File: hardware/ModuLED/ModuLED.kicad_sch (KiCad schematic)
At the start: 0 parts

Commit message: kicad
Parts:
- added D1, D10, D11, D12, D13, D14, D15, D16, D17, D18, D19, D2, D20, D21, D22, D23, D24, D25, D26, D27, D28, D29, D3, D30, D31, D32, D33, D34, D35, D36, D37, D38, D39, D4, D40, D41, D42, D43, D44, D45, D46, D47, D48, D49, D5, D50, D51, D52, D53, D54, D55, D56, D6, D7, D8, D9: LED, LED_THT:LED_D3.0mm_Clear, symbol Device:LED
- added U1: MAX7219, symbol Driver_LED:MAX7219
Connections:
- new net: D1.2 (A), D2.2 (A), D3.2 (A), D4.2 (A), D5.2 (A), D6.2 (A), D7.2 (A)
- new net: D29.2 (A), D30.2 (A), D31.2 (A), D32.2 (A), D33.2 (A), D34.2 (A), D35.2 (A)
- new net: D16.1 (K), D2.1 (K), D23.1 (K), D30.1 (K), D37.1 (K), D44.1 (K), D51.1 (K), D9.1 (K)
- new net: D15.2 (A), D16.2 (A), D17.2 (A), D18.2 (A), D19.2 (A), D20.2 (A), D21.2 (A)
- new net: D22.2 (A), D23.2 (A), D24.2 (A), D25.2 (A), D26.2 (A), D27.2 (A), D28.2 (A)
- new net: D50.2 (A), D51.2 (A), D52.2 (A), D53.2 (A), D54.2 (A), D55.2 (A), D56.2 (A)
- new net: D1.1 (K), D15.1 (K), D22.1 (K), D29.1 (K), D36.1 (K), D43.1 (K), D50.1 (K), D8.1 (K)
- new net: D43.2 (A), D44.2 (A), D45.2 (A), D46.2 (A), D47.2 (A), D48.2 (A), D49.2 (A)
- new net: D36.2 (A), D37.2 (A), D38.2 (A), D39.2 (A), D40.2 (A), D41.2 (A), D42.2 (A)
- new net: D10.2 (A), D11.2 (A), D12.2 (A), D13.2 (A), D14.2 (A), D8.2 (A), D9.2 (A)
- new net: U1.4 (GND), U1.9 (GND)

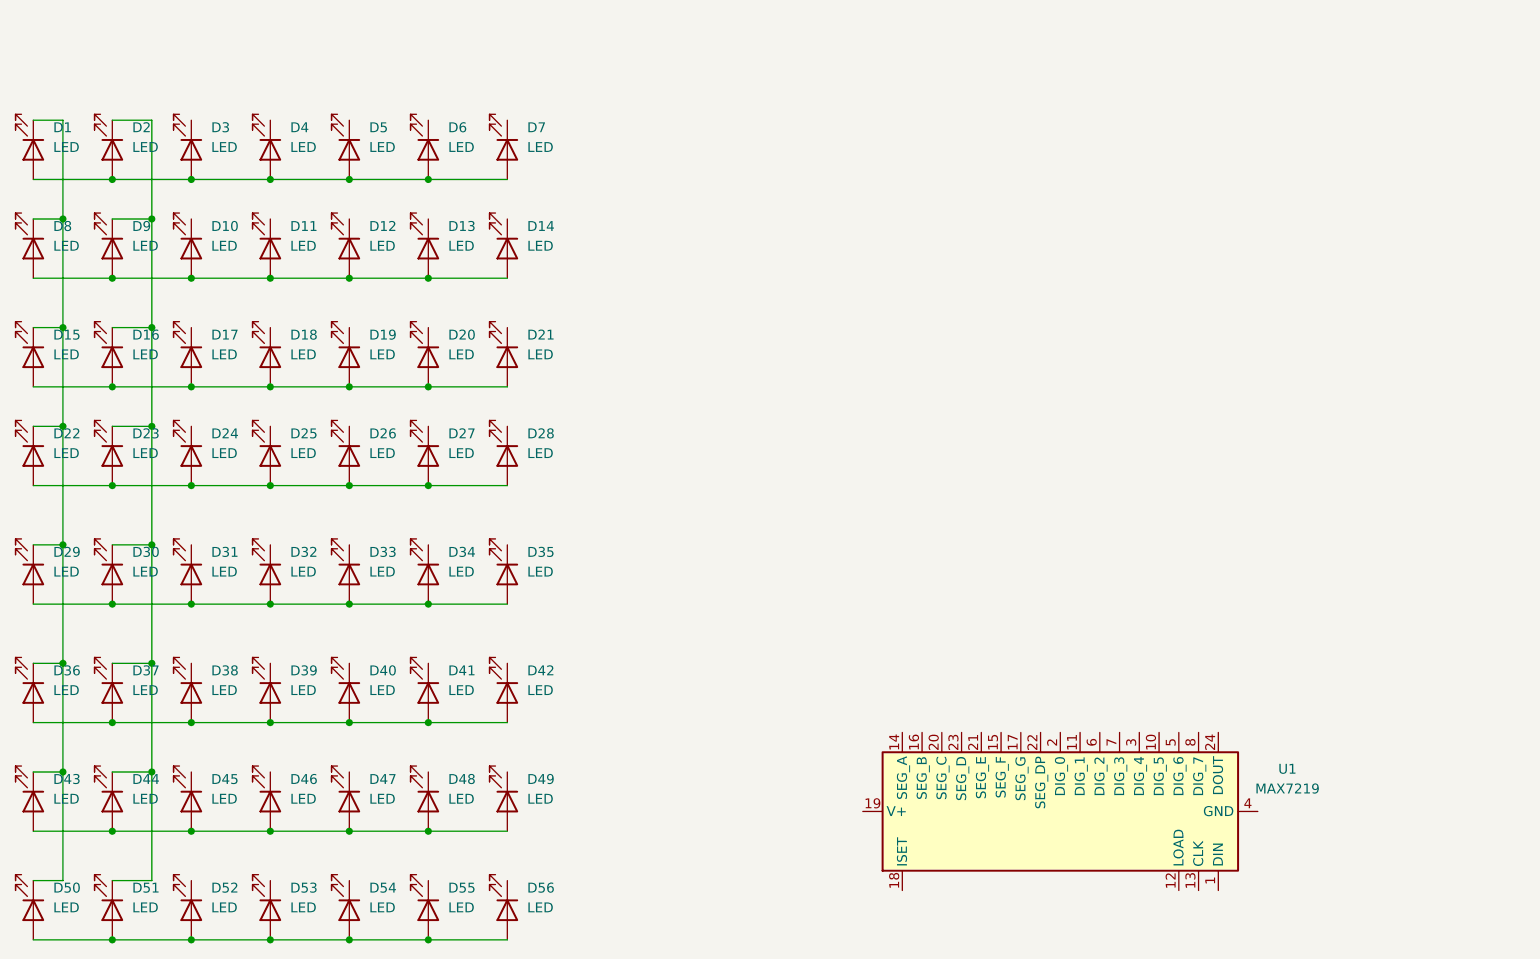
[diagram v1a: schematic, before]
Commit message: Diseño
Se sumo el esquemático y huella del display 1088 y arme un nuevo proyecto en kiCAD para ver como conectar los pines en la primera version de la placa
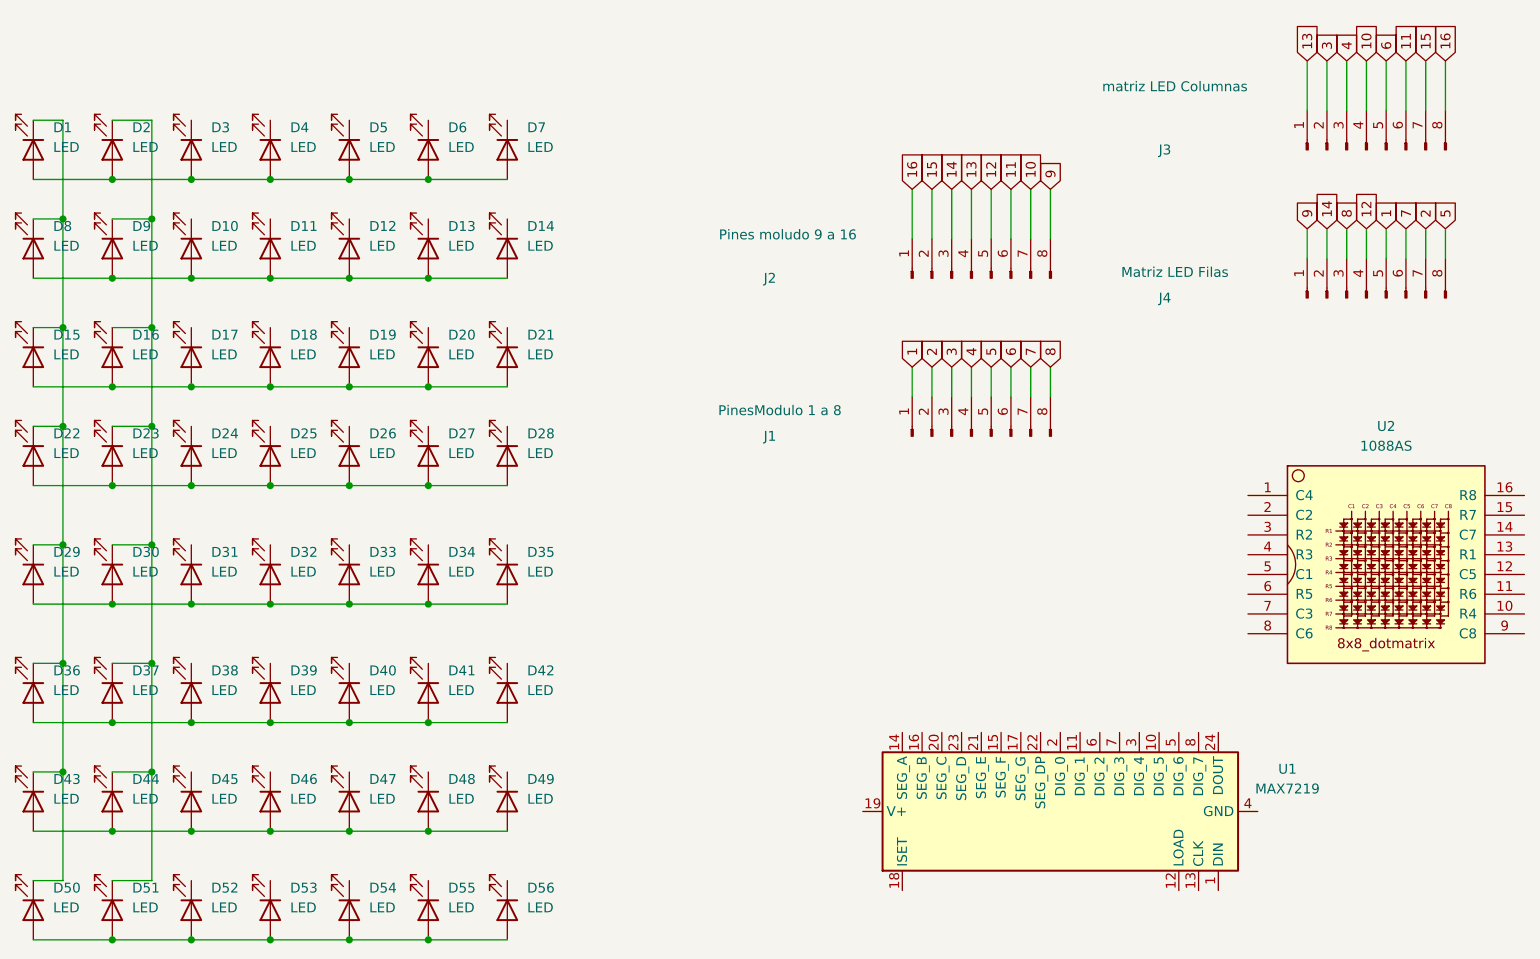
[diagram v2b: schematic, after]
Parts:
- added J1: PinesModulo 1 a 8, Connector_Hirose:Hirose_DF13-08P-1.25DSA_1x08_P1.25mm_Vertical, symbol Connector:Conn_01x08_Pin
- added J2: Pines moludo 9 a 16, Connector_Hirose:Hirose_DF13-08P-1.25DSA_1x08_P1.25mm_Vertical, symbol Connector:Conn_01x08_Pin
- added J3: matriz LED Columnas, Connector_Hirose:Hirose_DF13-08P-1.25DSA_1x08_P1.25mm_Vertical, symbol Connector:Conn_01x08_Pin
- added J4: Matriz LED Filas, Connector_Hirose:Hirose_DF13-08P-1.25DSA_1x08_P1.25mm_Vertical, symbol Connector:Conn_01x08_Pin
- added U2: 1088AS, lib_fp:LED_1088_Pin_Header, symbol LED_1088as:1088AS
- U1: footprint (none) -> Package_DIP:DIP-24_W7.62mm
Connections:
- new net 1: J1.1 (Pin_1), J4.5 (Pin_5)
- new net 10: J2.7 (Pin_7), J3.4 (Pin_4)
- new net 11: J2.6 (Pin_6), J3.6 (Pin_6)
- new net 12: J2.5 (Pin_5), J4.4 (Pin_4)
- new net 13: J2.4 (Pin_4), J3.1 (Pin_1)
- new net 14: J2.3 (Pin_3), J4.2 (Pin_2)
- new net 15: J2.2 (Pin_2), J3.7 (Pin_7)
- new net 16: J2.1 (Pin_1), J3.8 (Pin_8)
- new net 2: J1.2 (Pin_2), J4.7 (Pin_7)
- new net 3: J1.3 (Pin_3), J3.2 (Pin_2)
- new net 4: J1.4 (Pin_4), J3.3 (Pin_3)
- new net 5: J1.5 (Pin_5), J4.8 (Pin_8)
- new net 6: J1.6 (Pin_6), J3.5 (Pin_5)
- new net 7: J1.7 (Pin_7), J4.6 (Pin_6)
- new net 8: J1.8 (Pin_8), J4.3 (Pin_3)
- new net 9: J2.8 (Pin_8), J4.1 (Pin_1)
